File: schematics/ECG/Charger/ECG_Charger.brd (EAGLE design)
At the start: 11.6 x 27.7 mm, 11 parts, among them IC1 MCP73832_SOT23-5

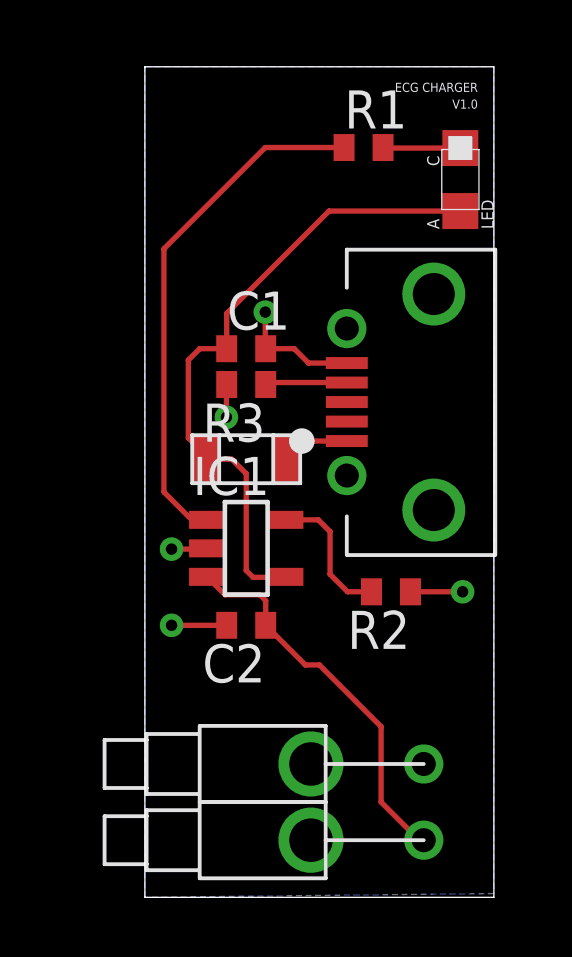
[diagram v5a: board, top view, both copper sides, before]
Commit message: using corrected piston package
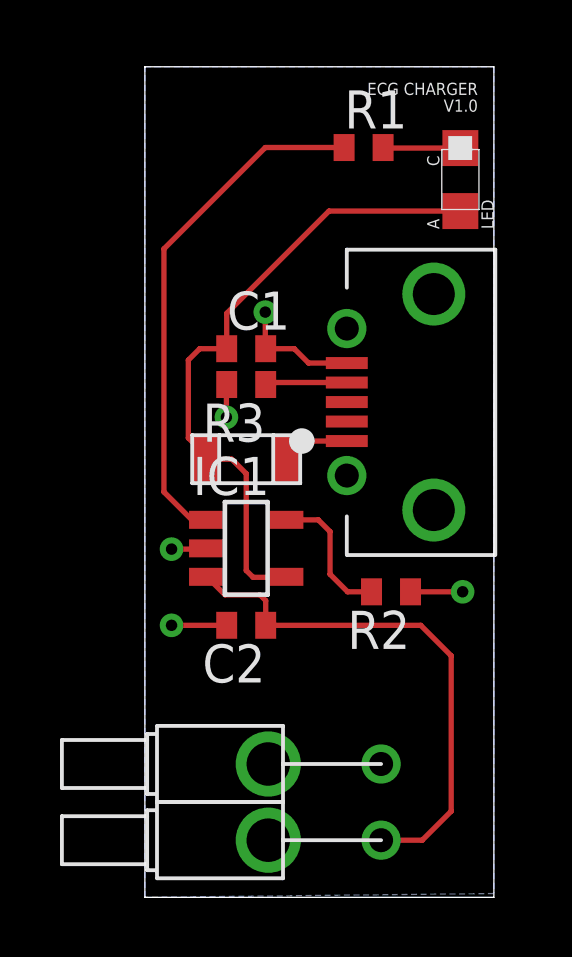
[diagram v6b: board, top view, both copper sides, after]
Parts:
- moved CONN1 1.42 mm to (2.54, 4.45)
- moved CONN2 1.42 mm to (2.54, 1.91)
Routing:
- net BATT: track 12.8 -> 17.6 mm
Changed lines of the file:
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@@
 <?xml version="1.0" encoding="utf-8"?>
 <!DOCTYPE eagle SYSTEM "eagle.dtd">
-<eagle version="6.5.0">
+<eagle version="6.4">
 <drawing>
 <settings>
@@
 <layer number="47" name="Measures" color="7" fill="1" visible="no" active="yes"/>
 <layer number="48" name="Document" color="7" fill="1" visible="yes" active="yes"/>
-<layer number="49" name="Reference" color="7" fill="1" visible="yes" active="yes"/>
+<layer number="49" name="Reference" color="7" fill="1" visible="no" active="yes"/>
 <layer number="50" name="dxf" color="7" fill="1" visible="no" active="no"/>
 <layer number="51" name="tDocu" color="7" fill="1" visible="yes" active="yes"/>
@@
 <wire x1="11.6332" y1="27.686" x2="0" y2="27.686" width="0" layer="20"/>
 <wire x1="0" y1="27.686" x2="0" y2="0" width="0" layer="20"/>
-<text x="11.0998" y="27.1526" size="0.3048" layer="21" rot="R180">ECG CHARGER</text>
-<text x="11.0998" y="26.5938" size="0.3048" layer="21" rot="R180">V1.0</text>
+<text x="11.0998" y="27.1526" size="0.4064" layer="21" rot="R180">ECG CHARGER</text>
+<text x="11.0998" y="26.5938" size="0.4064" layer="21" rot="R180">V1.0</text>
 </plain>
 <attributes>
@@
 <element name="FUSE" library="bourns-fuse" package="1206" value="FUSE-MF_SERIES" x="3.3782" y="14.605" rot="R180"/>
 <element name="C2" library="rcl" package="C0402" value="4.7uF" x="3.3782" y="9.0678" rot="R180"/>
-<element name="CONN2" library="pins" package="PISTON_RA_TH" value="PISTON_RA_TH" x="3.9624" y="1.905" rot="R180"/>
-<element name="CONN1" library="pins" package="PISTON_RA_TH" value="PISTON_RA_TH" x="3.9624" y="4.445" rot="R180"/>
+<element name="CONN2" library="pins" package="PISTON_RA_TH" value="PISTON_RA_TH" x="2.54" y="1.905" rot="R180"/>
+<element name="CONN1" library="pins" package="PISTON_RA_TH" value="PISTON_RA_TH" x="2.54" y="4.445" rot="R180"/>
 <element name="CONN3" library="KomodoOpenLab" package="USB_MICROB_FEMALE_RA_SMT" value="USB_MICROC" x="9.271" y="16.51" rot="R90">
 <attribute name="DIGIKEY" value="WM1399CT-ND" x="9.271" y="16.51" size="1.778" layer="27" rot="R90" display="off"/>
@@
 <contactref element="C2" pad="1"/>
 <contactref element="CONN2" pad="1"/>
-<wire x1="9.2964" y1="1.905" x2="9.144" y2="1.905" width="0.1778" layer="1"/>
-<wire x1="9.144" y1="1.905" x2="7.874" y2="3.175" width="0.1778" layer="1"/>
-<wire x1="7.874" y1="3.175" x2="7.874" y2="5.6896" width="0.1778" layer="1"/>
-<wire x1="7.874" y1="5.6896" x2="5.8166" y2="7.747" width="0.1778" layer="1"/>
 <wire x1="4.0282" y1="9.0678" x2="4.0282" y2="9.891" width="0.1778" layer="1"/>
 <wire x1="4.0282" y1="9.891" x2="3.8354" y2="10.0838" width="0.1778" layer="1"/>
 <wire x1="3.8354" y1="10.0838" x2="2.6716" y2="10.0838" width="0.1778" layer="1"/>
 <wire x1="2.6716" y1="10.0838" x2="2.0722" y2="10.6832" width="0.1778" layer="1"/>
-<wire x1="5.8166" y1="7.747" x2="5.349" y2="7.747" width="0.1778" layer="1"/>
-<wire x1="5.349" y1="7.747" x2="4.0282" y2="9.0678" width="0.1778" layer="1"/>
+<wire x1="7.874" y1="1.905" x2="9.2456" y2="1.905" width="0.1778" layer="1"/>
+<wire x1="9.2456" y1="1.905" x2="10.2108" y2="2.8702" width="0.1778" layer="1"/>
+<wire x1="10.2108" y1="2.8702" x2="10.2108" y2="8.0518" width="0.1778" layer="1"/>
+<wire x1="10.2108" y1="8.0518" x2="9.1948" y2="9.0678" width="0.1778" layer="1"/>
+<wire x1="9.1948" y1="9.0678" x2="4.0282" y2="9.0678" width="0.1778" layer="1"/>
 </signal>
 <signal name="N$1">
